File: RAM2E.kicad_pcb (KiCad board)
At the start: 4 copper layers, 78.2 x 50 mm, 59 parts, among them J1 AppleIIeAux, J2 JTAG, U1 5M240ZT100, U2 W9812G6KH-6, U3 74LVC245, U4 74LVC245, U5 74LVC245, U6 74AHCT245, U7 74AHCT245, U8 XC6206P332MR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

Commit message: Actually fabbed 10/6/2020
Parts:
- U1: value 5M240ZT100 -> 5M240ZT100C5N
- U3, U4, U5: value 74LVC245 -> 74LVC245APW
- U6, U7: value 74AHCT245 -> 74AHCT245PW
- renumbered C12 to C25

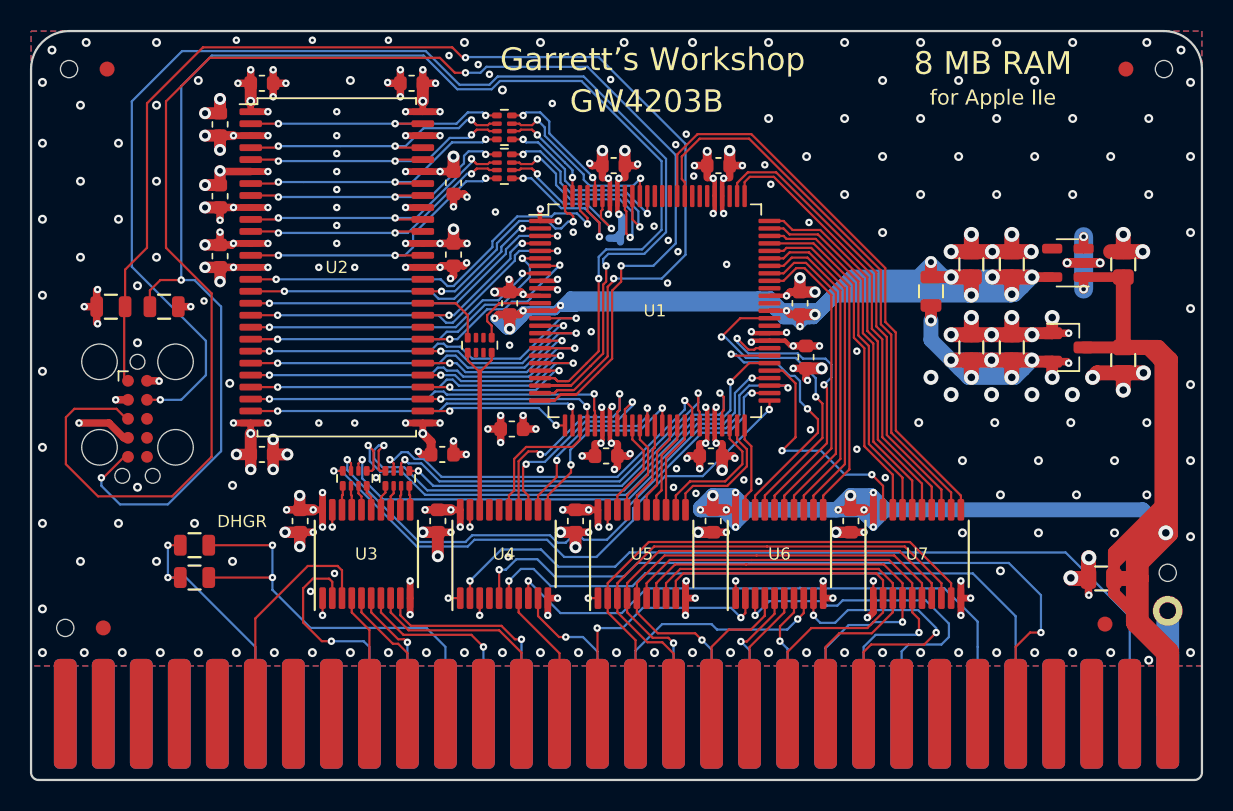
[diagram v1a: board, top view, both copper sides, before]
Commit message: Added C14M buffering and header
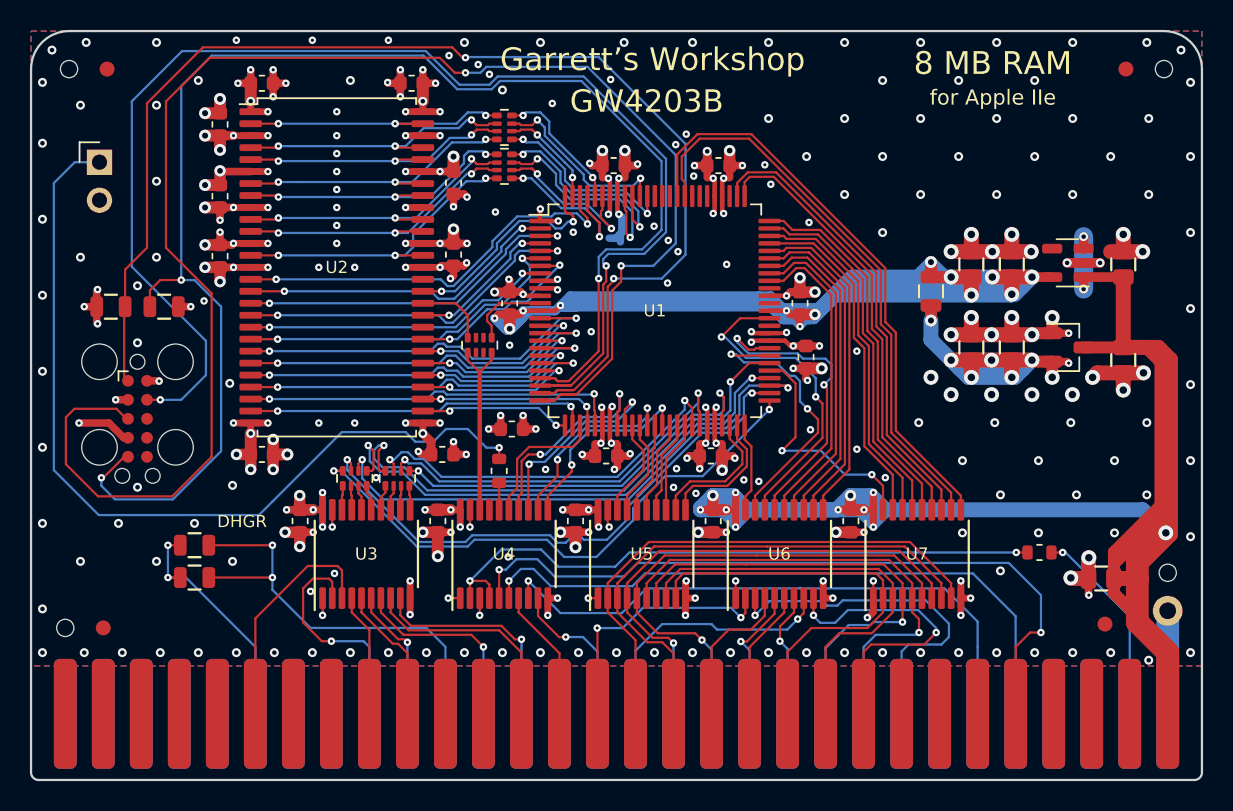
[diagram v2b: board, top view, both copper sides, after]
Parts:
- added J3: C14M, Connector_PinHeader_2.54mm:PinHeader_1x02_P2.54mm_Vertical, F.Cu at (202.9, 98.4)
- added R2: 33, stdpads:R_0603, F.Cu at (265.8, 124.5)
- added R3: 33, stdpads:R_0603, F.Cu at (229.7, 119.0)
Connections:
- U4 pad 2: /C14M -> /C14MR
- U4 pad 4: GND -> /C14MR
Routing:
- net /C14MB: track 0.00 -> 58.0 mm, vias 0 -> 1
- net /C14MR: track 0.00 -> 42.4 mm, vias 0 -> 2
- net /C14M: track 55.2 -> 13.5 mm
- net Net-(R3-Pad2): track 0.00 -> 1.80 mm
- net GND: track 162.7 -> 161.8 mm, vias 294 -> 291
- net +3V3: track 121.4 -> 121.3 mm, vias 79 -> 78
